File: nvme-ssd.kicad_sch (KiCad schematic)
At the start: 20 parts, among them J3 1-2199230-6

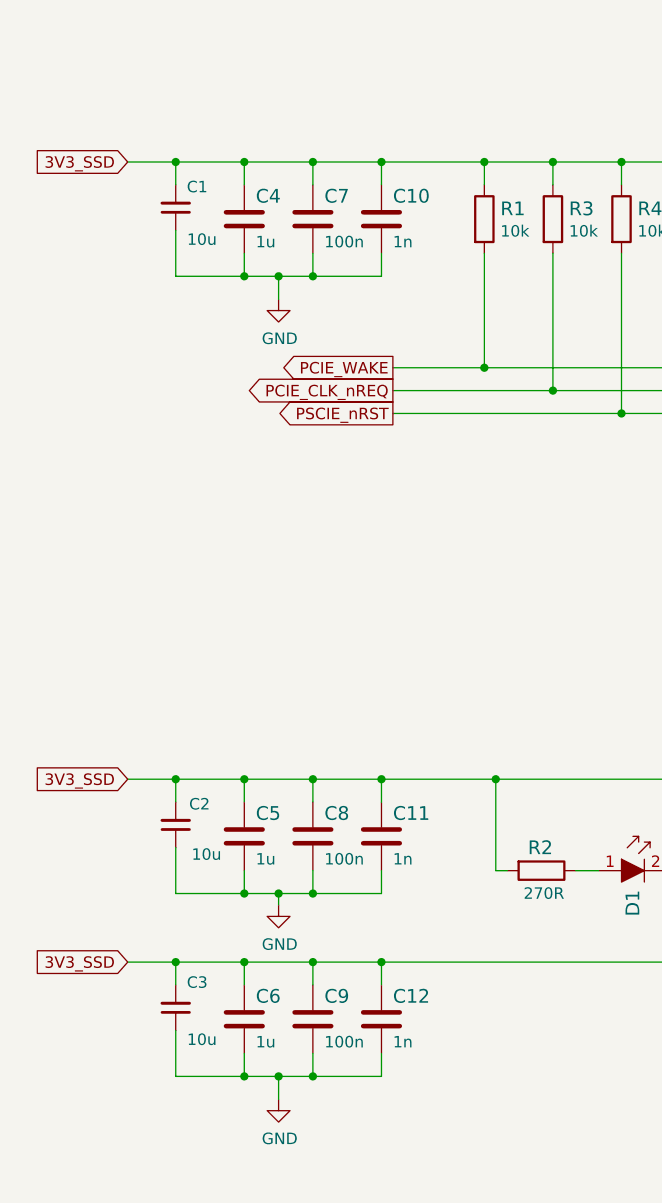
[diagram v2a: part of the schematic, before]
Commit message: Update C4 C5 C6 symbol and footprint
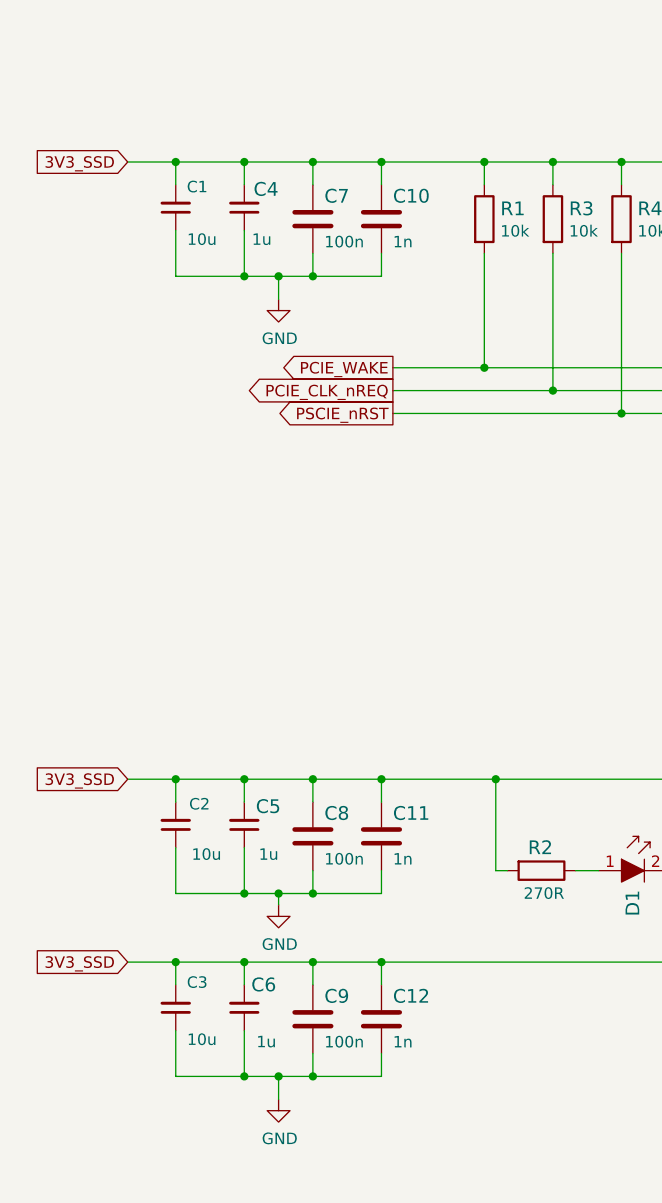
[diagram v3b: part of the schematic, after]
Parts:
- C4, C5, C6: footprint scalenode-cm4-baseboard-footprints:0603-cap -> antmicro-footprints:C_0603_1608Metric; symbol scalenode-cm4-baseboard:C_1u_0603 -> antmicroCapacitors0603:C_1u_0603; Author (none) -> Antmicro; License (none) -> Apache-2.0; Manufacturer WALSIN -> Walsin
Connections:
- net 3V3_SSD: now also C4.2, C5.2, C6.2; no longer C4.1, C5.1, C6.1
- net GND: now also C4.1, C5.1, C6.1; no longer C4.2, C5.2, C6.2
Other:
- moved on the sheet: C4, C5, C6

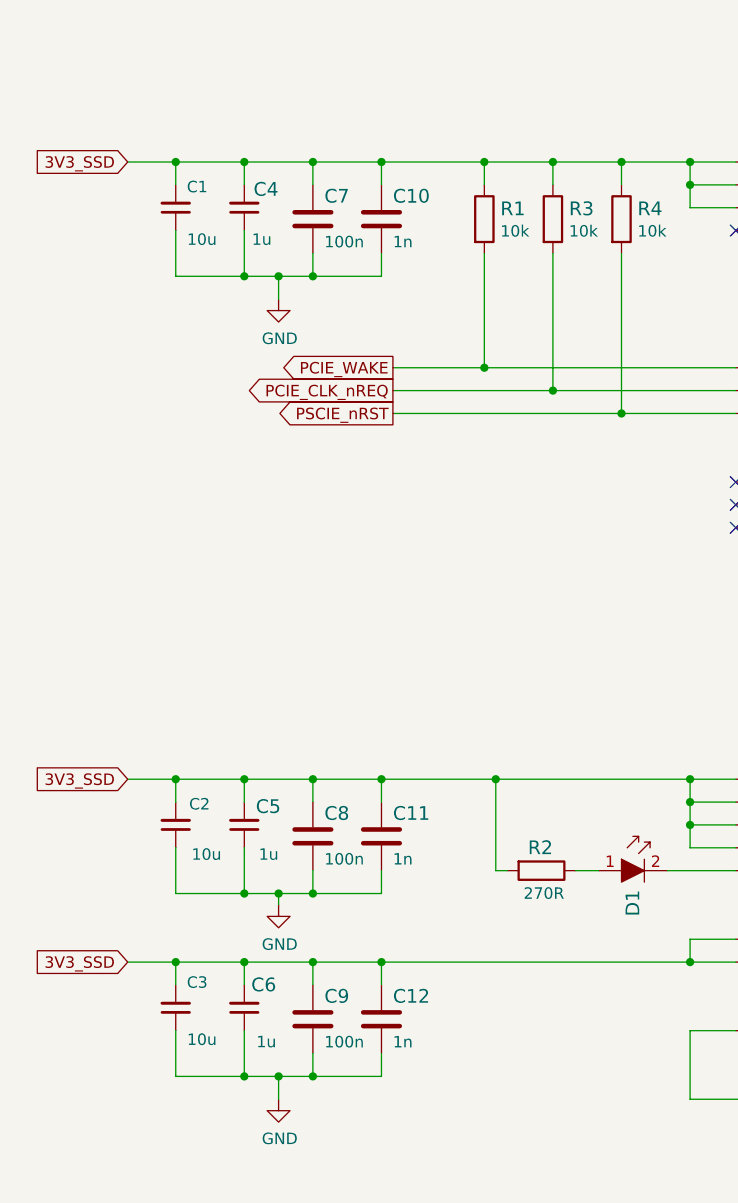
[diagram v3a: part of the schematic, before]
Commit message: Update C7 C8 C9 symbol and footprint
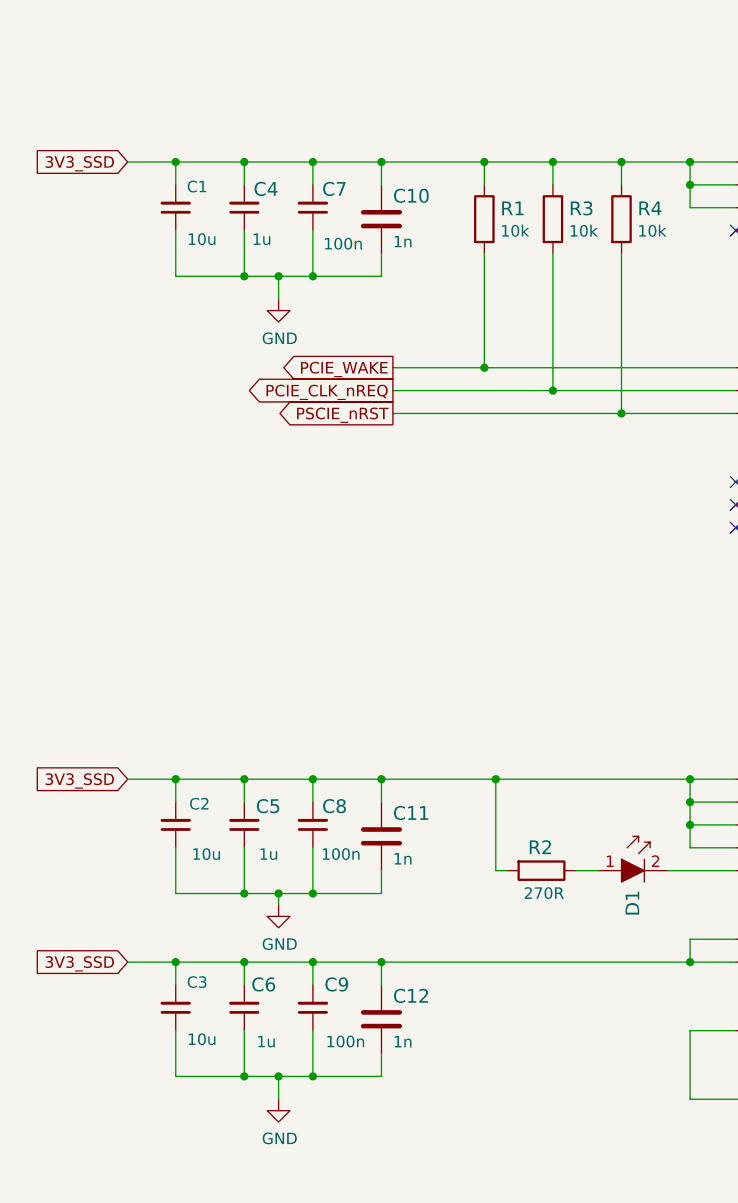
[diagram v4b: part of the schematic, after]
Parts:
- C7, C8, C9: footprint scalenode-cm4-baseboard-footprints:0603-cap -> antmicro-footprints:C_0603_1608Metric; symbol scalenode-cm4-baseboard:C_100n_0603 -> antmicroCapacitors0603:C_100n_0603; Author (none) -> Antmicro; License (none) -> Apache-2.0
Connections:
- net 3V3_SSD: now also C7.2, C8.2, C9.2; no longer C7.1, C8.1, C9.1
- net GND: now also C7.1, C8.1, C9.1; no longer C7.2, C8.2, C9.2
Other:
- moved on the sheet: C7, C8, C9
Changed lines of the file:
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@@
+    (stroke (width 0) (type default) (color 0 0 0 0))
+  )
+  (wire (pts (xy 86.36 133.35) (xy 86.36 135.89))
     (stroke (width 0) (type default) (color 0 0 0 0))
   )
@@
     (stroke (width 0) (type default) (color 0 0 0 0))
   )
-  (wire (pts (xy 86.36 135.89) (xy 86.36 133.35))
-    (stroke (width 0) (type default) (color 0 0 0 0))
-  )
   (wire (pts (xy 128.27 133.35) (xy 128.27 130.81))
     (stroke (width 0) (type default) (color 0 0 0 0))
@@
     (stroke (width 0) (type default) (color 0 0 0 0))
   )
+  (wire (pts (xy 86.36 113.03) (xy 86.36 115.57))
+    (stroke (width 0) (type default) (color 0 0 0 0))
+  )
   (wire (pts (xy 171.45 49.53) (xy 181.61 49.53))
     (stroke (width 0) (type default) (color 0 0 0 0))
@@
     (stroke (width 0) (type default) (color 0 0 0 0))
   )
-  (wire (pts (xy 86.36 54.61) (xy 86.36 57.15))
+  (wire (pts (xy 86.36 52.07) (xy 86.36 57.15))
     (stroke (width 0) (type default) (color 0 0 0 0))
   )
@@
     (stroke (width 0) (type default) (color 0 0 0 0))
   )
-  (wire (pts (xy 86.36 123.19) (xy 86.36 125.73))
-    (stroke (width 0) (type default) (color 0 0 0 0))
-  )
   (wire (pts (xy 113.03 44.45) (xy 105.41 44.45))
     (stroke (width 0) (type default) (color 0 0 0 0))
@@
     (stroke (width 0) (type default) (color 0 0 0 0))
   )
-  (wire (pts (xy 86.36 115.57) (xy 86.36 113.03))
+  (wire (pts (xy 86.36 120.65) (xy 86.36 125.73))
     (stroke (width 0) (type default) (color 0 0 0 0))
   )
@@
     (stroke (width 0) (type default) (color 0 0 0 0))
   )
-  (wire (pts (xy 86.36 143.51) (xy 86.36 146.05))
+  (wire (pts (xy 86.36 140.97) (xy 86.36 146.05))
     (stroke (width 0) (type default) (color 0 0 0 0))
   )
@@
     (stroke (width 0) (type default) (color 0 0 0 0))
   )
-  (wire (pts (xy 86.36 46.99) (xy 86.36 44.45))
+  (wire (pts (xy 86.36 44.45) (xy 86.36 46.99))
     (stroke (width 0) (type default) (color 0 0 0 0))
   )
@@
     (pin "2")
   )
-  (symbol (lib_id "scalenode-cm4-baseboard:C_100n_0603") (at 86.36 119.38 0) (unit 1)
+  (symbol (lib_id "antmicroCapacitors0603:C_100n_0603") (at 86.36 120.65 90) (unit 1)
     (in_bom yes) (on_board yes)
-    (property "Reference" "C8" (id 0) (at 87.63 116.84 0)
+    (property "Reference" "C8" (id 0) (at 90.17 116.078 90)
       (effects (font (size 1.524 1.524)) (justify left))
     )
-    (property "Value" "C_100n_0603" (id 1) (at 86.36 123.19 0)
+    (property "Value" "C_100n_0603" (id 1) (at 90.17 120.65 0)
       (effects (font (size 1.524 1.524)) hide)
     )
-    (property "Footprint" "scalenode-cm4-baseboard-footprints:0603-cap" (id 2) (at 91.44 114.3 0)
-      (effects (font (size 1.524 1.524)) (justify left) hide)
-    )
-    (property "Datasheet" "" (id 3) (at 86.36 119.38 0)
-      (effects (font (size 1.27 1.27)) hide)
-    )
-    (property "Manufacturer" "AVX" (id 4) (at 91.44 109.22 0)
-      (effects (font (size 1.524 1.524)) (justify left) hide)
-    )
-    (property "MPN" "0603YC104KAZ2A" (id 5) (at 91.44 111.76 0)
-      (effects (font (size 1.524 1.524)) (justify left) hide)
-    )
-    (property "Val" "100n" (id 6) (at 87.63 121.92 0)
-      (effects (font (size 1.27 1.27)) (justify left))
+    (property "Footprint" "antmicro-footprints:C_0603_1608Metric" (id 2) (at 99.06 100.33 0)
+      (effects (font (size 1.27 1.27) (thickness 0.15)) (justify left bottom) hide)
+    )
+    (property "Datasheet" " " (id 3) (at 101.6 100.33 0)
+      (effects (font (size 1.27 1.27) (thickness 0.15)) (justify left bottom) hide)
+    )
+    (property "Manufacturer" "AVX" (id 4) (at 106.68 100.33 0)
+      (effects (font (size 1.27 1.27) (thickness 0.15)) (justify left bottom) hide)
+    )
+    (property "MPN" "0603YC104KAZ2A" (id 5) (at 104.14 100.33 0)
+      (effects (font (size 1.27 1.27) (thickness 0.15)) (justify left bottom) hide)
+    )
+    (property "Val" "100n" (id 6) (at 91.694 120.65 90)
+      (effects (font (size 1.27 1.27) (thickness 0.15)) (justify left bottom))
+    )
+    (property "License" "Apache-2.0" (id 7) (at 109.22 100.33 0)
+      (effects (font (size 1.27 1.27) (thickness 0.15)) (justify left bottom) hide)
+    )
+    (property "Author" "Antmicro" (id 8) (at 111.76 100.33 0)
+      (effects (font (size 1.27 1.27) (thickness 0.15)) (justify left bottom) hide)
+    )
+    (property "Voltage" "" (id 9) (at 114.3 100.33 0)
+      (effects (font (size 1.27 1.27)) (justify left bottom) hide)
+    )
+    (property "Dielectric" "" (id 10) (at 116.84 100.33 0)
+      (effects (font (size 1.27 1.27)) (justify left bottom) hide)
     )
     (pin "1")
@@
     (pin "2")
   )
-  (symbol (lib_id "scalenode-cm4-baseboard:C_100n_0603") (at 86.36 139.7 0) (unit 1)
+  (symbol (lib_id "antmicroCapacitors0603:C_100n_0603") (at 86.36 140.97 90) (unit 1)
     (in_bom yes) (on_board yes)
-    (property "Reference" "C9" (id 0) (at 87.63 137.16 0)
+    (property "Reference" "C9" (id 0) (at 90.424 135.89 90)
       (effects (font (size 1.524 1.524)) (justify left))
     )
-    (property "Value" "C_100n_0603" (id 1) (at 86.36 143.51 0)
+    (property "Value" "C_100n_0603" (id 1) (at 90.17 140.97 0)
       (effects (font (size 1.524 1.524)) hide)
     )
-    (property "Footprint" "scalenode-cm4-baseboard-footprints:0603-cap" (id 2) (at 91.44 134.62 0)
-      (effects (font (size 1.524 1.524)) (justify left) hide)
-    )
-    (property "Datasheet" "" (id 3) (at 86.36 139.7 0)
-      (effects (font (size 1.27 1.27)) hide)
-    )
-    (property "Manufacturer" "AVX" (id 4) (at 91.44 129.54 0)
-      (effects (font (size 1.524 1.524)) (justify left) hide)
-    )
-    (property "MPN" "0603YC104KAZ2A" (id 5) (at 91.44 132.08 0)
-      (effects (font (size 1.524 1.524)) (justify left) hide)
-    )
-    (property "Val" "100n" (id 6) (at 87.63 142.24 0)
-      (effects (font (size 1.27 1.27)) (justify left))
+    (property "Footprint" "antmicro-footprints:C_0603_1608Metric" (id 2) (at 99.06 120.65 0)
+      (effects (font (size 1.27 1.27) (thickness 0.15)) (justify left bottom) hide)
+    )
+    (property "Datasheet" " " (id 3) (at 101.6 120.65 0)
+      (effects (font (size 1.27 1.27) (thickness 0.15)) (justify left bottom) hide)
+    )
+    (property "Manufacturer" "AVX" (id 4) (at 106.68 120.65 0)
+      (effects (font (size 1.27 1.27) (thickness 0.15)) (justify left bottom) hide)
+    )
+    (property "MPN" "0603YC104KAZ2A" (id 5) (at 104.14 120.65 0)
+      (effects (font (size 1.27 1.27) (thickness 0.15)) (justify left bottom) hide)
+    )
+    (property "Val" "100n" (id 6) (at 92.202 141.478 90)
+      (effects (font (size 1.27 1.27) (thickness 0.15)) (justify left bottom))
+    )
+    (property "License" "Apache-2.0" (id 7) (at 109.22 120.65 0)
+      (effects (font (size 1.27 1.27) (thickness 0.15)) (justify left bottom) hide)
+    )
+    (property "Author" "Antmicro" (id 8) (at 111.76 120.65 0)
+      (effects (font (size 1.27 1.27) (thickness 0.15)) (justify left bottom) hide)
+    )
+    (property "Voltage" "" (id 9) (at 114.3 120.65 0)
+      (effects (font (size 1.27 1.27)) (justify left bottom) hide)
+    )
+    (property "Dielectric" "" (id 10) (at 116.84 120.65 0)
+      (effects (font (size 1.27 1.27)) (justify left bottom) hide)
     )
     (pin "1")
@@
     (pin "2")
   )
-  (symbol (lib_id "scalenode-cm4-baseboard:C_100n_0603") (at 86.36 50.8 0) (unit 1)
+  (symbol (lib_id "antmicroCapacitors0603:C_100n_0603") (at 86.36 52.07 90) (unit 1)
     (in_bom yes) (on_board yes)
-    (property "Reference" "C7" (id 0) (at 87.63 48.26 0)
+    (property "Reference" "C7" (id 0) (at 90.17 47.498 90)
       (effects (font (size 1.524 1.524)) (justify left))
     )
-    (property "Value" "C_100n_0603" (id 1) (at 86.36 54.61 0)
+    (property "Value" "C_100n_0603" (id 1) (at 90.17 52.07 0)
       (effects (font (size 1.524 1.524)) hide)
     )
-    (property "Footprint" "scalenode-cm4-baseboard-footprints:0603-cap" (id 2) (at 91.44 45.72 0)
-      (effects (font (size 1.524 1.524)) (justify left) hide)
-    )
-    (property "Datasheet" "" (id 3) (at 86.36 50.8 0)
-      (effects (font (size 1.27 1.27)) hide)
-    )
-    (property "Manufacturer" "AVX" (id 4) (at 91.44 40.64 0)
-      (effects (font (size 1.524 1.524)) (justify left) hide)
-    )
-    (property "MPN" "0603YC104KAZ2A" (id 5) (at 91.44 43.18 0)
-      (effects (font (size 1.524 1.524)) (justify left) hide)
-    )
-    (property "Val" "100n" (id 6) (at 87.63 53.34 0)
-      (effects (font (size 1.27 1.27)) (justify left))
+    (property "Footprint" "antmicro-footprints:C_0603_1608Metric" (id 2) (at 99.06 31.75 0)
+      (effects (font (size 1.27 1.27) (thickness 0.15)) (justify left bottom) hide)
+    )
+    (property "Datasheet" " " (id 3) (at 101.6 31.75 0)
+      (effects (font (size 1.27 1.27) (thickness 0.15)) (justify left bottom) hide)
+    )
+    (property "Manufacturer" "AVX" (id 4) (at 106.68 31.75 0)
+      (effects (font (size 1.27 1.27) (thickness 0.15)) (justify left bottom) hide)
+    )
+    (property "MPN" "0603YC104KAZ2A" (id 5) (at 104.14 31.75 0)
+      (effects (font (size 1.27 1.27) (thickness 0.15)) (justify left bottom) hide)
+    )
+    (property "Val" "100n" (id 6) (at 91.948 52.832 90)
+      (effects (font (size 1.27 1.27) (thickness 0.15)) (justify left bottom))
+    )
+    (property "License" "Apache-2.0" (id 7) (at 109.22 31.75 0)
+      (effects (font (size 1.27 1.27) (thickness 0.15)) (justify left bottom) hide)
+    )
+    (property "Author" "Antmicro" (id 8) (at 111.76 31.75 0)
+      (effects (font (size 1.27 1.27) (thickness 0.15)) (justify left bottom) hide)
+    )
+    (property "Voltage" "" (id 9) (at 114.3 31.75 0)
+      (effects (font (size 1.27 1.27)) (justify left bottom) hide)
+    )
+    (property "Dielectric" "" (id 10) (at 116.84 31.75 0)
+      (effects (font (size 1.27 1.27)) (justify left bottom) hide)
     )
     (pin "1")

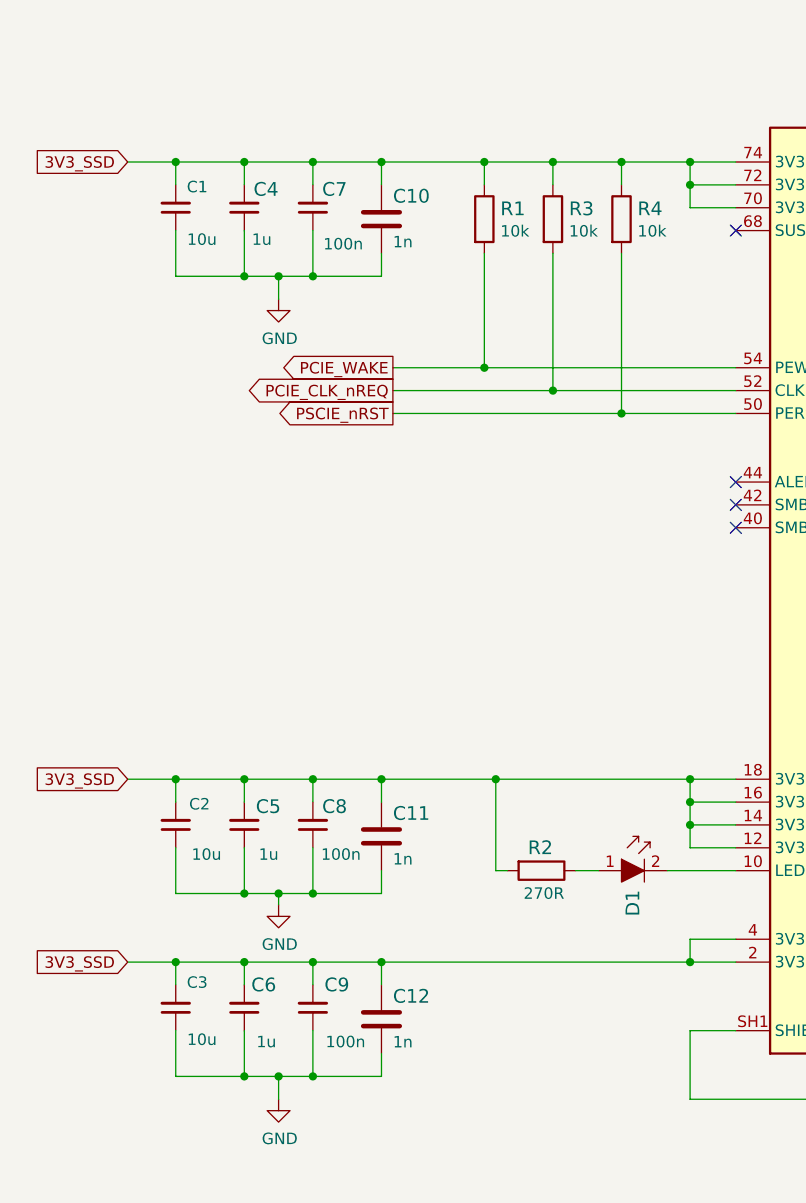
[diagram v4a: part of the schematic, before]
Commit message: Update C10 C11 C12 symbols and footprints
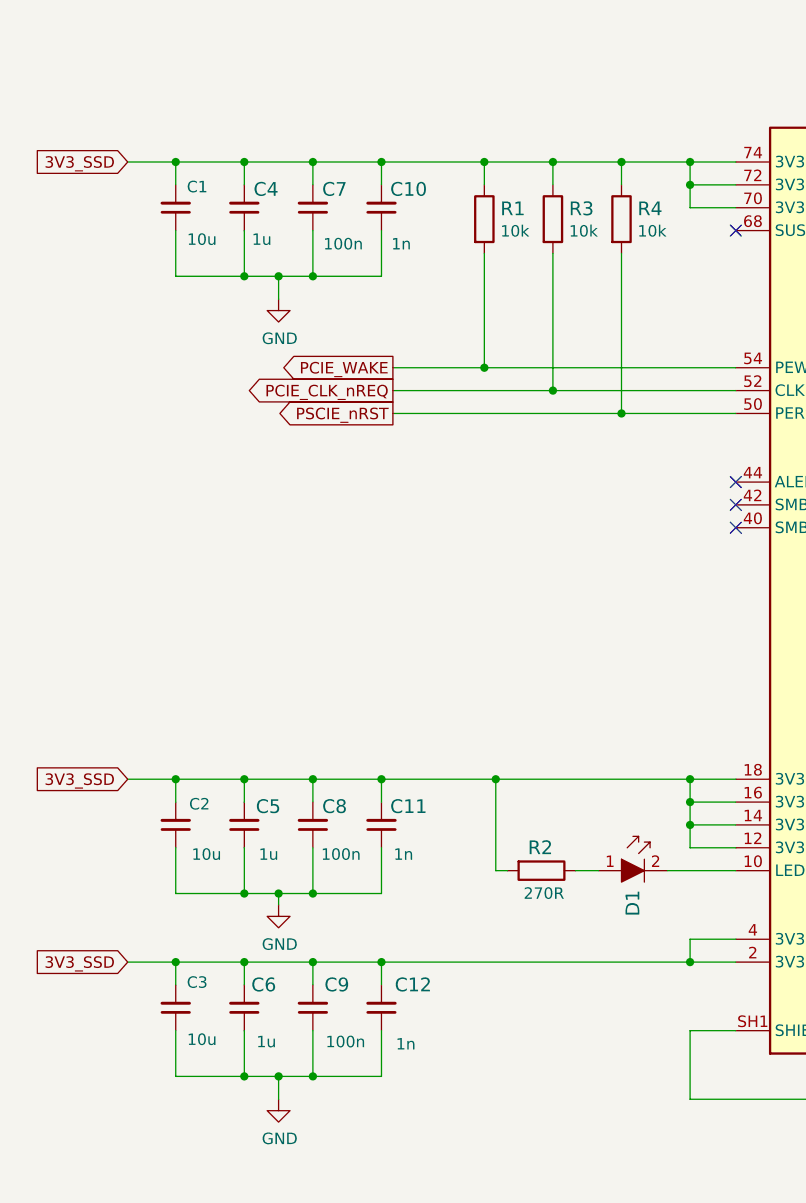
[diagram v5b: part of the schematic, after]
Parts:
- C10, C11, C12: footprint scalenode-cm4-baseboard-footprints:0603-cap -> antmicro-footprints:C_0603_1608Metric; symbol scalenode-cm4-baseboard:C_1n_0603 -> antmicroCapacitors0603:C_1n_0603; Author (none) -> Antmicro; License (none) -> Apache-2.0
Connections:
- net 3V3_SSD: now also C10.2, C11.2, C12.2; no longer C10.1, C11.1, C12.1
- net GND: now also C10.1, C11.1, C12.1; no longer C10.2, C11.2, C12.2
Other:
- moved on the sheet: C10, C11, C12
